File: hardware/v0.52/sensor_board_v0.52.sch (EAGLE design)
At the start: 48 parts, among them J3 USB-MICROB, U1 ATMEGA328P, U2 TSL2561, U3 OPA344, U4 RFM69HW, U5 FT231XS, U6 ADMP401, U7 SHT31-DIS, U8 MCP1703CB, U9 BMP280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

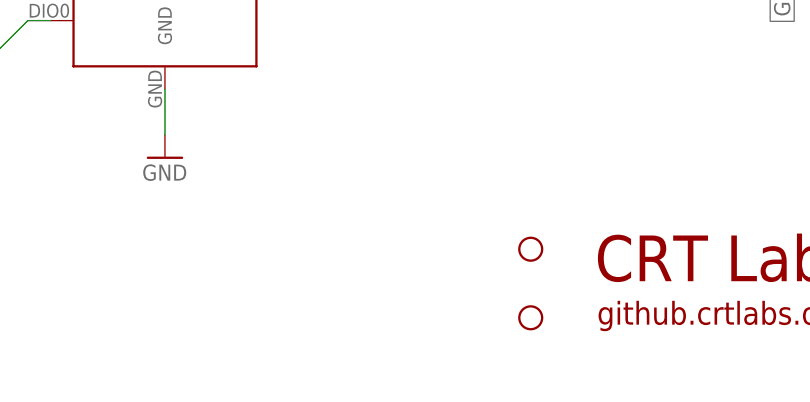
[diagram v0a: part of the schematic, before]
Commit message: Added fiducial markers on PCB
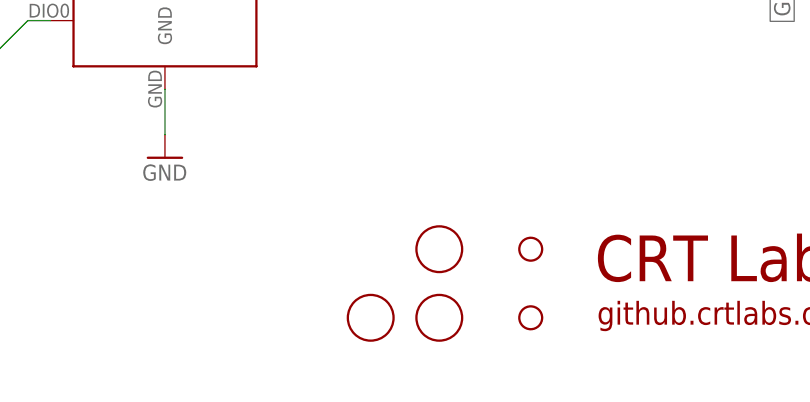
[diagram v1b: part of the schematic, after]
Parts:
- added U$1, U$2, U$3: FIDUCIAL, adafruit:FIDUCIAL
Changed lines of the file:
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@@
 <part name="JP2" library="adafruit" deviceset="PINHD-1X1" device=""/>
 <part name="FRAME1" library="SparkFun-Retired" deviceset="FRAME-A3" device=""/>
+<part name="U$1" library="adafruit" deviceset="FIDUCIAL" device=""/>
+<part name="U$2" library="adafruit" deviceset="FIDUCIAL" device=""/>
+<part name="U$3" library="adafruit" deviceset="FIDUCIAL" device=""/>
 </parts>
 <sheets>
@@
 <instance part="JP2" gate="G$1" x="170.18" y="-53.34" rot="R90"/>
 <instance part="FRAME1" gate="G$1" x="-71.12" y="-116.84"/>
+<instance part="U$1" gate="G$1" x="175.26" y="-99.06"/>
+<instance part="U$2" gate="G$1" x="175.26" y="-106.68"/>
+<instance part="U$3" gate="G$1" x="167.64" y="-106.68"/>
 </instances>
 <busses>
